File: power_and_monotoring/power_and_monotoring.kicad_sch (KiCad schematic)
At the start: 4 parts

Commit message: Final
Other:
- sheet Connectors ports: added none; removed BSPD_24V, DATALOGGER_24V
- sheet feather ports: added BSPD_TRIGGER; removed D_BSPD_TRIGGER
- sheet fuses ports: added none; removed BSPD_24V, DATA_LOGGER_24V
- sheet logic ports: added +3.3V, 12V; removed D_BSPD_TRIGGER

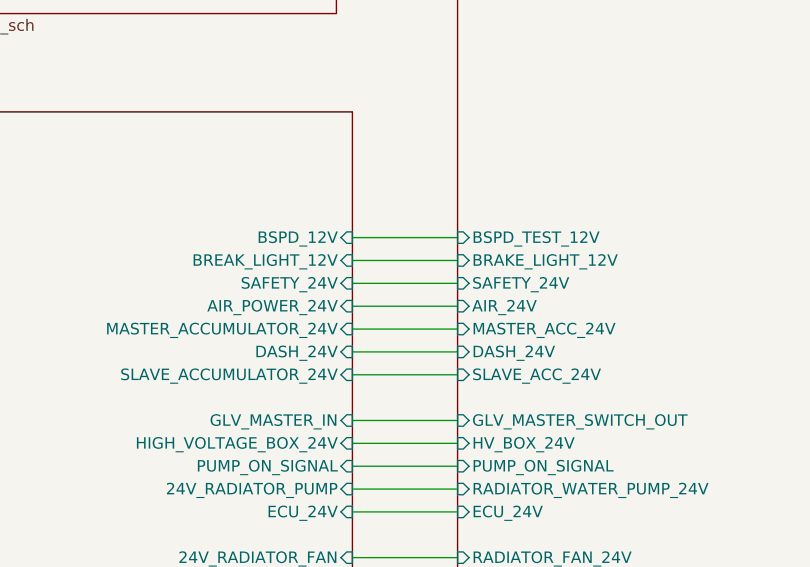
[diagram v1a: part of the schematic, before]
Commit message: Made it 4 layers
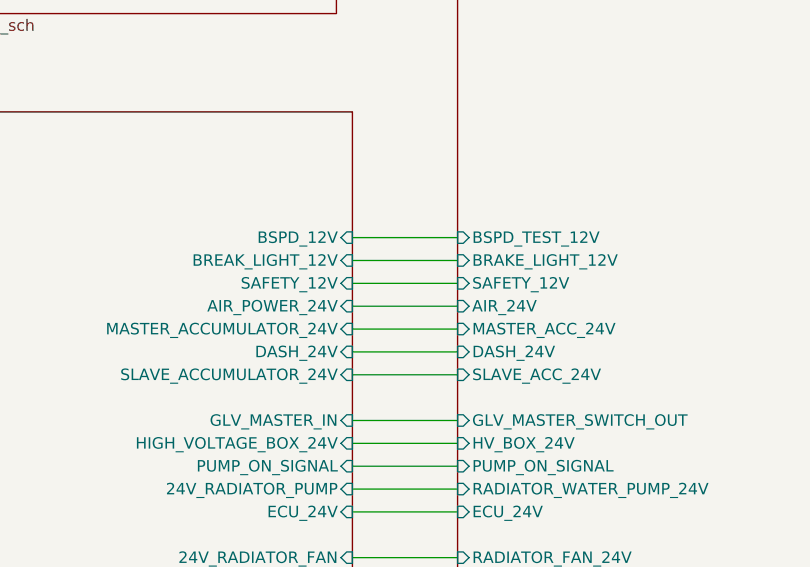
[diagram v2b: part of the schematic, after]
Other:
- sheet Connectors ports: added SAFETY_12V; removed SAFETY_24V
- sheet fuses ports: added SAFETY_12V; removed SAFETY_24V
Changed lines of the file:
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@@
-			)
-		)
-		(pin "SAFETY_24V" input
-			(at 153.416 167.64 0)
-			(effects
-				(font
-					(size 1.27 1.27)
-				)
-				(justify right)
 			)
 		)
@@
 		(pin "BSPD_12V" input
 			(at 153.416 162.56 0)
+			(effects
+				(font
+					(size 1.27 1.27)
+				)
+				(justify right)
+			)
+		)
+		(pin "SAFETY_12V" input
+			(at 153.416 167.64 0)
 			(effects
 				(font
@@
 			)
 		)
-		(pin "SAFETY_24V" input
-			(at 165.1 167.64 180)
-			(effects
-				(font
-					(size 1.27 1.27)
-				)
-				(justify left)
-			)
-		)
 		(pin "HV_BOX_24V" input
 			(at 165.1 185.42 180)
@@
 			(effects
 				(font
+					(size 1.27 1.27)
+				)
+				(justify left)
+			)
+		)
+		(pin "SAFETY_12V" input
+			(at 165.1 167.64 180)
+			(effects
+				(font
